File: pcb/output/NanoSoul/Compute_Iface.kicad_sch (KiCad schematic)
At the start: 2 parts

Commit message: pcb: 3mm 白边 + J2/J7 离 J4 + DRC 丝印告警清零
- 最外围 3mm 白边：板放大到 94×92（Ø108 切边收小到 7/8mm），铜/器件焊盘距最外缘 ≥3mm
  （自动布线内缩 3mm；顶排 J5/J6 下移、J8 左移退出白边区）。
- J2/J7 离 J4：右月牙整体右移 1.6mm，离 J4 本体 +0.83mm（原相擦 0.78mm）。
- DRC = 0 warning：5 个位号(D4/D5/Q1/U1/U7)挪开、接线图例升到 0.8mm 并缩短、
  删 J3/J4 压挖孔丝印、隐藏 6 安装孔与 U7 位号。
- 17.8mm 母座行距核对通过；4 个 M3 安装孔成规则 54×82 矩形（旧版钉在 Ø108 圆外、钻不出，已修正）。
- 余 MOT_RTN/GND 各 1 段跨挖孔大电流网/地：按 docs 铁律出板前人工绕挖孔补（GND 建议铺地铜），
  网表连接关系正确（其余 170 网 0 短路）。原理图 ERC 不适用：circuit-synth 开源导出无导线、
  网表为真值源。详见 docs/05 §9.1。
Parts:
- J3, J4: footprint Connector_PinHeader_2.54mm:PinHeader_1x20_P2.54mm_Vertical -> Connector_PinSocket_2.54mm:PinSocket_1x20_P2.54mm_Vertical; hierarchy_path /8a83f0c7-8320-4874-8ea1-ef8ee28a330a/ef3f754e-c23c-4762-9d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 -> /cc6d016d-315a-4023-b551-816edf85e992/d132638e-f658-47d9-9b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; root_uuid 8a83f0c7-8320-4874-8ea1-ef8ee28a330a -> cc6d016d-315a-4023-b551-816edf85e992
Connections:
- net I2C1_SCL: now also J4.7 (Pin_7); no longer J4.9 (Pin_9)
- net I2C1_SDA: now also J4.6 (Pin_6); no longer J4.7 (Pin_7)
- net IMU_CS: now also J4.9 (Pin_9); no longer J3.2 (Pin_2)
- net IMU_INT: now also J4.10 (Pin_10); no longer J3.1 (Pin_1)
- net IMU_MISO: now also J3.10 (Pin_10); no longer J3.9 (Pin_9)
- net IMU_MOSI: now also J3.9 (Pin_9); no longer J3.10 (Pin_10)
- net IMU_SCLK: now also J3.2 (Pin_2); no longer J4.20 (Pin_20)
- net M1_ENC_A: now also J3.7 (Pin_7); no longer J4.15 (Pin_15)
- net M1_ENC_B: now also J3.6 (Pin_6); no longer J4.16 (Pin_16)
- net M2_IN2: now also J4.15 (Pin_15); no longer J3.7 (Pin_7)
- net MOTOR_STBY: now also J3.1 (Pin_1); no longer J3.6 (Pin_6)
- net MOT_ISENSE: now also J4.16 (Pin_16); no longer J4.6 (Pin_6)
- net P4_GPIO23: now also J4.20 (Pin_20); no longer J4.10 (Pin_10)

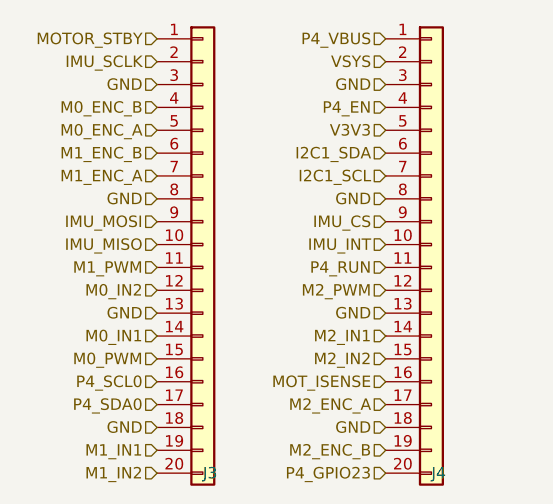
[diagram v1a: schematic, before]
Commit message: pcb: schematic-parity 真零(零 ignore) + 重导 Gerber
DRC `--schematic-parity --severity-all` = 0 violation / 0 unconnected /
0 schematic-parity,62 项检查全置 error、零 ignore(旧版的 7 项 ignore 全部真修掉,
非关检查)。verify_board 65/65、布线 778 走线+60 过孔未动。

- 修通 circuit-synth 原理图连通性:它把一器件所有网名标签堆在 pin1 → KiCad 推断错网。
  按 .net 逐脚在真实连接点重放 global_label(fix_sch_labels),net_conflict 199→0;
  真 NC 脚在板上配同名 unconnected- 网对齐(assign_nc_nets)。
- 板 Value 回填真实值(顺修「板上 Value=封装名」的 BOM bug)、lib_id 去库前缀(fix_board_meta);
  原理图删 circuit-synth 私有字段/封装过滤器、补缺失 Value(fix_sch_fields);
  J2 attr→through_hole(USB-C 靠屏蔽脚 THT 安装,属实);4×M3 孔标 board_only。
- 唯一保留例外 = J2(USB-C)连接器内部 DRU(实测 0.10mm 铜/0.185mm 孔,JLC 可造;
  KiCad 官方 USB_C_Receptacle_HRO 封装内部孔距也仅 0.15mm → 换封装消不掉、
  改窄焊盘会伤实焊。限 J2 内部两两对象,不放宽对板上走线)。
- 重导 Gerber(9 层 Protel 扩展名 + Excellon 钻孔)+ BOM/CPL。
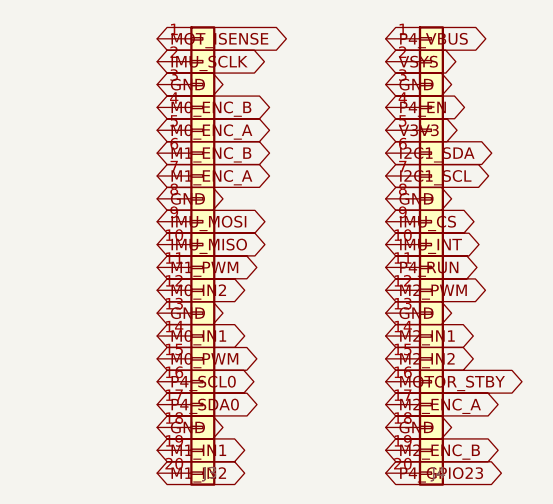
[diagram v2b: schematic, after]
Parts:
- J3, J4: value (none) -> PinSocket_1x20_P2.54mm_Vertical; footprint Connector_PinSocket_2.54mm:PinSocket_1x20_P2.54mm_Vertical -> PinSocket_1x20_P2.54mm_Vertical; hierarchy_path /cc6d016d-315a-4023-b551-816edf85e992/d132638e-f658-47d9-9b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 -> (none); project_name NanoSoul -> (none); root_uuid cc6d016d-315a-4023-b551-816edf85e992 -> (none)
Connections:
- net MOTOR_STBY: now also J4.16 (Pin_16); no longer J3.1 (Pin_1)
- net MOT_ISENSE: now also J3.1 (Pin_1); no longer J4.16 (Pin_16)
